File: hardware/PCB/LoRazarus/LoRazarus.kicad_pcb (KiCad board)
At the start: 2 copper layers, 44 parts, among them J1 S2B-PH-SM4-TB_LF__SN_, J2 S2B-PH-SM4-TB_LF__SN_, J3 Conn_01x02_Pin, J4 Conn_ARM_SWD_TagConnect_TC203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, Q1 AO3401A, Q2 MMBT3906, Q3 MMBT3904, Q4 MMBT3904, U1 STM32L031K6Tx, U2 TPS7A0230PDBVR, U3 TLV3691IDCKR, U4 MAX9634HEUK+T

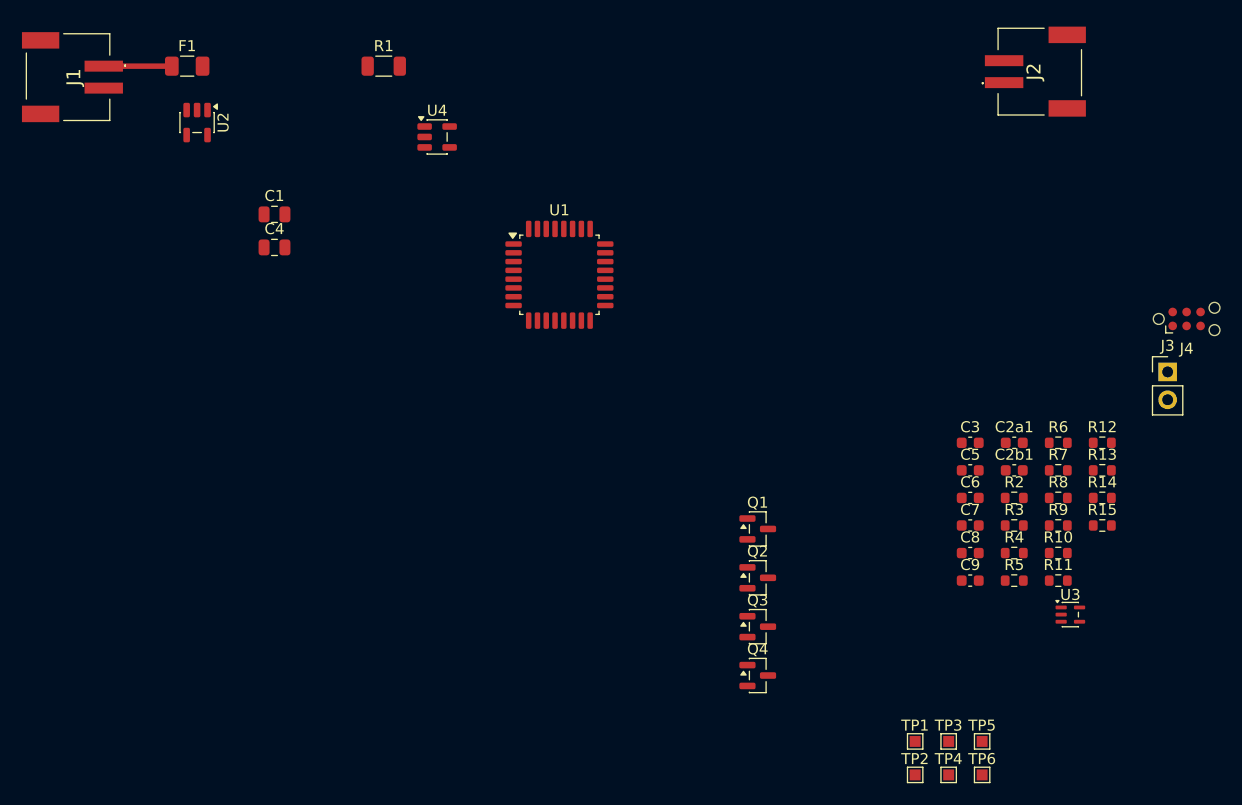
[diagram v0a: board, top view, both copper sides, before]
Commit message: LoRazarus pcb layout finished
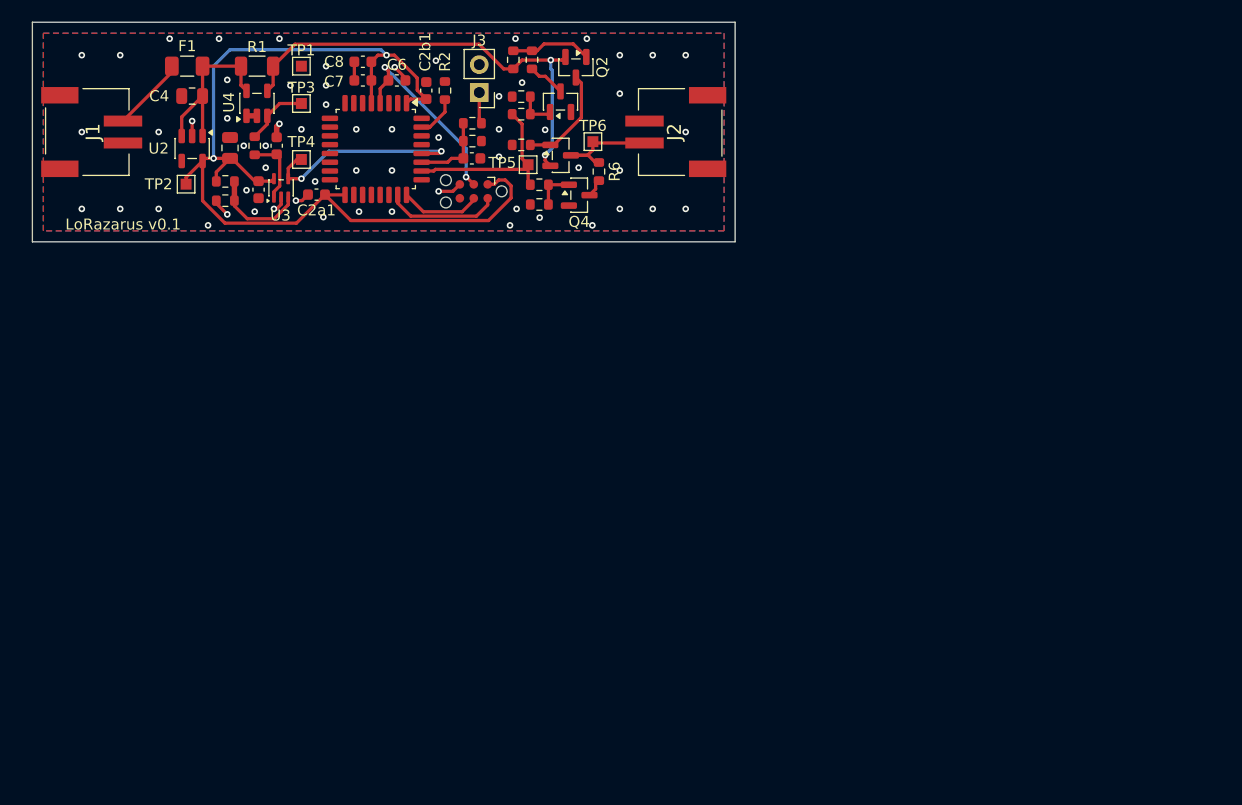
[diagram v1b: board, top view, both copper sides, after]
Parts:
- moved TP2 85.5 mm to (71.0, 69.8)
- moved TP1 83.1 mm to (81.5, 59.0)
- moved TP3 82.8 mm to (81.5, 62.4)
- moved U3 81.7 mm to (79.7, 70.1), turned to 90 degrees
- moved TP4 81.3 mm to (81.5, 67.5)
- moved R8 79.9 mm to (77.2, 66.2), turned to -90 degrees
- moved R4 78.7 mm to (74.6, 71.2), turned to 180 degrees
- moved R3 78.4 mm to (74.6, 69.5)
- moved C8 71.1 mm to (87.1, 58.6), turned to 180 degrees
- moved C5 69.7 mm to (77.6, 70.2), turned to -90 degrees
- moved C3 68.7 mm to (79.2, 66.2), turned to 90 degrees
- moved R11 68.7 mm to (100.8, 58.4), turned to 90 degrees
- moved C7 68.6 mm to (87.1, 60.3), turned to 180 degrees
- moved TP6 67.7 mm to (108.0, 65.9)
- moved J3 67.7 mm to (97.7, 61.4), turned to 180 degrees
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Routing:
- net VDD: track 0.00 -> 92.1 mm, vias 0 -> 2
- net VBATT_SENSED: track 0.00 -> 41.5 mm, vias 0 -> 2
- net COMPOUT: track 0.00 -> 19.3 mm, vias 0 -> 2
- net RESET: track 0.00 -> 17.9 mm, vias 0 -> 2
- net KILL: track 0.00 -> 17.2 mm
- net +BATT: track 0.00 -> 16.7 mm
- net GND: track 0.00 -> 13.6 mm, vias 0 -> 61
- net VBATT_OUT: track 0.00 -> 10.5 mm
- net SWDIO: track 0.00 -> 10.5 mm
- net SWSIG: track 0.00 -> 9.53 mm
- net Net-(U3-IN-): track 0.00 -> 8.84 mm
- net Net-(Q2-B): track 0.00 -> 7.40 mm
- net SWCLK: track 0.00 -> 7.37 mm
- net HBIN: track 0.00 -> 7.14 mm
- net Net-(U3-IN+): track 0.00 -> 6.25 mm
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- added copper zone on B.Cu, net GND
- added copper zone on F.Cu, net GND
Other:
- board outline added: 64 x 20 mm
- board text added: "LoRazarus v0.1"
